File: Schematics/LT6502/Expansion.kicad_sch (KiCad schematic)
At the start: 5 parts, among them J9 DIN41612_02x32_AC

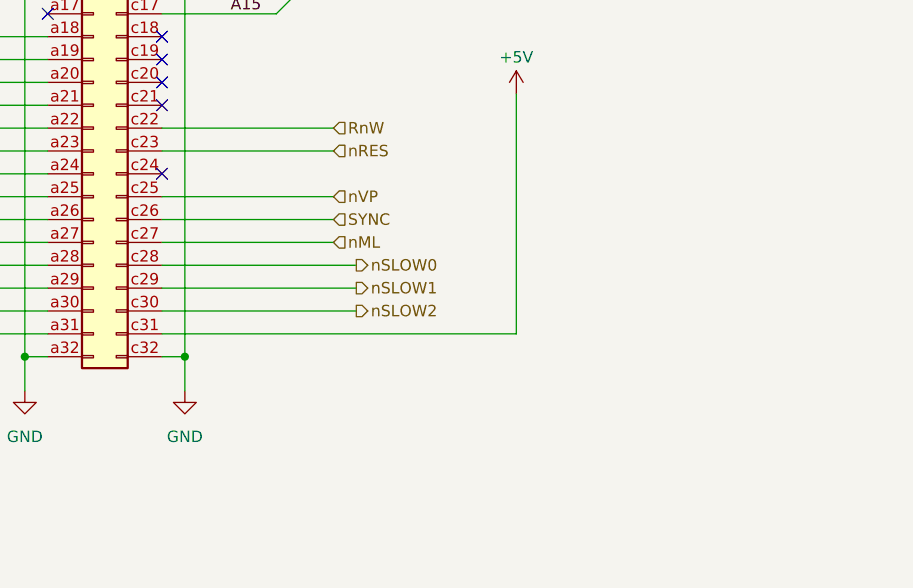
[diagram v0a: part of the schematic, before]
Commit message: Tweaks to Schematics
Shrunk main PCB
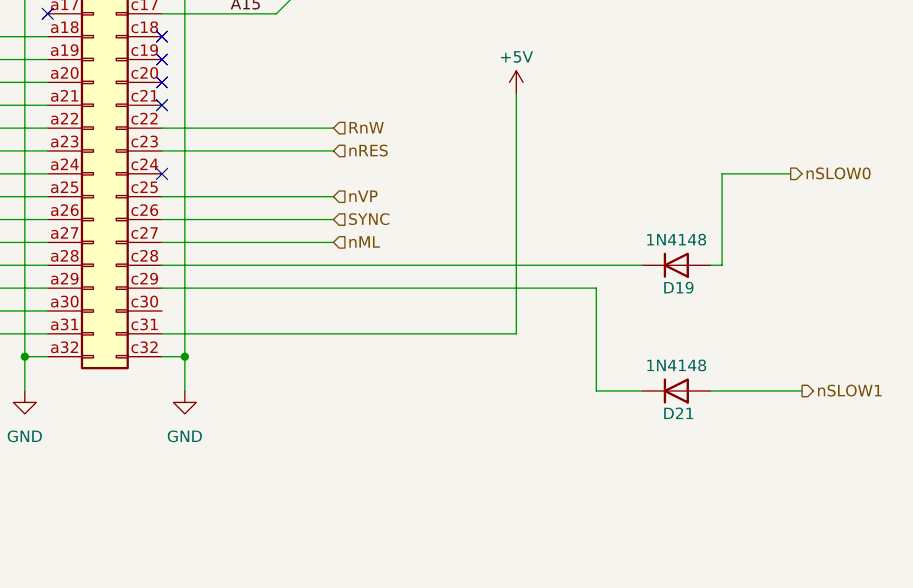
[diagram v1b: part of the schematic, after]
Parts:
- added D19, D21: 1N4148, Diode_THT:D_DO-35_SOD27_P7.62mm_Horizontal, symbol Diode:1N4148
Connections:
- net nSLOW0: now also D19.2 (A); no longer J9.c28 (Pin_c28)
- net nSLOW1: now also D21.2 (A); no longer J9.c29 (Pin_c29)
- net nSLOW2: no longer names the net of J9.c30 (Pin_c30)
- new net: D21.1 (K), J9.c29 (Pin_c29)
- new net: D19.1 (K), J9.c28 (Pin_c28)
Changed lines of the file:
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@@
 	(wire
 		(pts
-			(xy 182.88 124.46) (xy 161.29 124.46)
+			(xy 231.14 114.3) (xy 223.52 114.3)
 		)
 		(stroke
@@
 		)
 	)
-	(wire
-		(pts
-			(xy 182.88 129.54) (xy 161.29 129.54)
-		)
-		(stroke
-			(width 0)
-			(type default)
-		)
-	)
 	(bus
 		(pts
@@
 	(wire
 		(pts
-			(xy 182.88 127) (xy 161.29 127)
+			(xy 232.41 138.43) (xy 222.25 138.43)
 		)
 		(stroke
@@
 	(wire
 		(pts
+			(xy 209.55 138.43) (xy 209.55 127)
+		)
+		(stroke
+			(width 0)
+			(type default)
+		)
+	)
+	(wire
+		(pts
 			(xy 161.29 134.62) (xy 163.83 134.62)
 		)
@@
 	(wire
 		(pts
+			(xy 209.55 127) (xy 161.29 127)
+		)
+		(stroke
+			(width 0)
+			(type default)
+		)
+	)
+	(wire
+		(pts
 			(xy 163.83 134.62) (xy 163.83 55.88)
 		)
@@
 	(wire
 		(pts
+			(xy 214.63 124.46) (xy 161.29 124.46)
+		)
+		(stroke
+			(width 0)
+			(type default)
+		)
+	)
+	(wire
+		(pts
 			(xy 148.59 71.12) (xy 133.35 71.12)
 		)
@@
 	(wire
 		(pts
+			(xy 214.63 138.43) (xy 209.55 138.43)
+		)
+		(stroke
+			(width 0)
+			(type default)
+		)
+	)
+	(wire
+		(pts
 			(xy 180.34 119.38) (xy 161.29 119.38)
 		)
@@
 		)
 	)
+	(wire
+		(pts
+			(xy 223.52 114.3) (xy 223.52 124.46)
+		)
+		(stroke
+			(width 0)
+			(type default)
+		)
+	)
 	(bus
 		(pts
@@
 		(pts
 			(xy 133.35 111.76) (xy 148.59 111.76)
+		)
+		(stroke
+			(width 0)
+			(type default)
+		)
+	)
+	(wire
+		(pts
+			(xy 223.52 124.46) (xy 222.25 124.46)
 		)
 		(stroke
@@
 	(hierarchical_label "nSLOW0"
 		(shape output)
-		(at 182.88 124.46 0)
+		(at 231.14 114.3 0)
 		(effects
 			(font
@@
 	(hierarchical_label "nSLOW1"
 		(shape output)
-		(at 182.88 127 0)
+		(at 232.41 138.43 0)
 		(effects
 			(font
@@
 			)
 			(justify right)
-		)
-	)
-	(hierarchical_label "nSLOW2"
-		(shape output)
-		(at 182.88 129.54 0)
-		(effects
-			(font
-				(size 1.27 1.27)
-			)
-			(justify left)
 		)
 	)
@@
 	)
 	(symbol
+		(lib_id "Diode:1N4148")
+		(at 218.44 138.43 0)
+		(mirror x)
+		(unit 1)
+		(exclude_from_sim no)
+		(in_bom yes)
+		(on_board yes)
+		(dnp no)
+		(property "Reference" "D21"
+			(at 218.694 140.97 0)
+			(effects
+				(font
+					(size 1.27 1.27)
+				)
+			)
+		)
+		(property "Value" "1N4148"
+			(at 218.44 135.636 0)
+			(effects
+				(font
+					(size 1.27 1.27)
+				)
+			)
+		)
+		(property "Footprint" "Diode_THT:D_DO-35_SOD27_P7.62mm_Horizontal"
+			(at 218.44 138.43 0)
+			(effects
+				(font
+					(size 1.27 1.27)
+				)
+				(hide yes)
+			)
+		)
+		(property "Datasheet" "https://assets.nexperia.com/documents/data-sheet/1N4148_1N4448.pdf"
+			(at 218.44 138.43 0)
+			(effects
+				(font
+					(size 1.27 1.27)
+				)
+				(hide yes)
+			)
+		)
+		(property "Description" "100V 0.15A standard switching diode, DO-35"
+			(at 218.44 138.43 0)
+			(effects
+				(font
+					(size 1.27 1.27)
+				)
+				(hide yes)
+			)
+		)
+		(property "Sim.Device" "D"
+			(at 218.44 138.43 0)
+			(effects
+				(font
+					(size 1.27 1.27)
+				)
+				(hide yes)
+			)
+		)
+		(property "Sim.Pins" "1=K 2=A"
+			(at 218.44 138.43 0)
+			(effects
+				(font
+					(size 1.27 1.27)
+				)
+				(hide yes)
+			)
+		)
+		(pin "2"
+		)
+		(pin "1"
+		)
+		(instances
+			(project "LT6502"
+				(path "/a2243a34-697c-4939-97f7-df548e421864/813c43d1-5652-442b-96d1-062e6d70605b"
+					(reference "D22")
+					(unit 1)
+				)
+				(path "/a2243a34-697c-4939-97f7-df548e421864/e762d4e1-6eae-4d69-baef-1dedfb10bbd7"
+					(reference "D21")
+					(unit 1)
+				)
+			)
+		)
+	)
+	(symbol
 		(lib_id "Connector:DIN41612_02x32_AC")
 		(at 153.67 93.98 0)
@@
 					(unit 1)
 				)
+			)
+		)
+	)
+	(symbol
+		(lib_id "Diode:1N4148")
+		(at 218.44 124.46 0)
+		(mirror x)
+		(unit 1)
+		(exclude_from_sim no)
+		(in_bom yes)
+		(on_board yes)
+		(dnp no)
+		(property "Reference" "D19"
+			(at 218.694 127 0)
+			(effects
+				(font
+					(size 1.27 1.27)
+				)
+			)
+		)
+		(property "Value" "1N4148"
+			(at 218.44 121.666 0)
+			(effects
+				(font
+					(size 1.27 1.27)
+				)
+			)
+		)
+		(property "Footprint" "Diode_THT:D_DO-35_SOD27_P7.62mm_Horizontal"
+			(at 218.44 124.46 0)
+			(effects
+				(font
+					(size 1.27 1.27)
+				)
+				(hide yes)
+			)
+		)
+		(property "Datasheet" "https://assets.nexperia.com/documents/data-sheet/1N4148_1N4448.pdf"
+			(at 218.44 124.46 0)
+			(effects
+				(font
+					(size 1.27 1.27)
+				)
+				(hide yes)
+			)
+		)
+		(property "Description" "100V 0.15A standard switching diode, DO-35"
+			(at 218.44 124.46 0)
+			(effects
+				(font
+					(size 1.27 1.27)
+				)
+				(hide yes)
+			)
+		)
+		(property "Sim.Device" "D"
+			(at 218.44 124.46 0)
+			(effects
+				(font
+					(size 1.27 1.27)
+				)
+				(hide yes)
+			)
+		)
+		(property "Sim.Pins" "1=K 2=A"
+			(at 218.44 124.46 0)
+			(effects
+				(font
+					(size 1.27 1.27)
+				)
+				(hide yes)
+			)
+		)
+		(pin "2"
+		)
+		(pin "1"
+		)
+		(instances
+			(project "LT6502"
+				(path "/a2243a34-697c-4939-97f7-df548e421864/813c43d1-5652-442b-96d1-062e6d70605b"
+					(reference "D20")
+					(unit 1)
+				)
+				(path "/a2243a34-697c-4939-97f7-df548e421864/e762d4e1-6eae-4d69-baef-1dedfb10bbd7"
+					(reference "D19")
+					(unit 1)
+				)

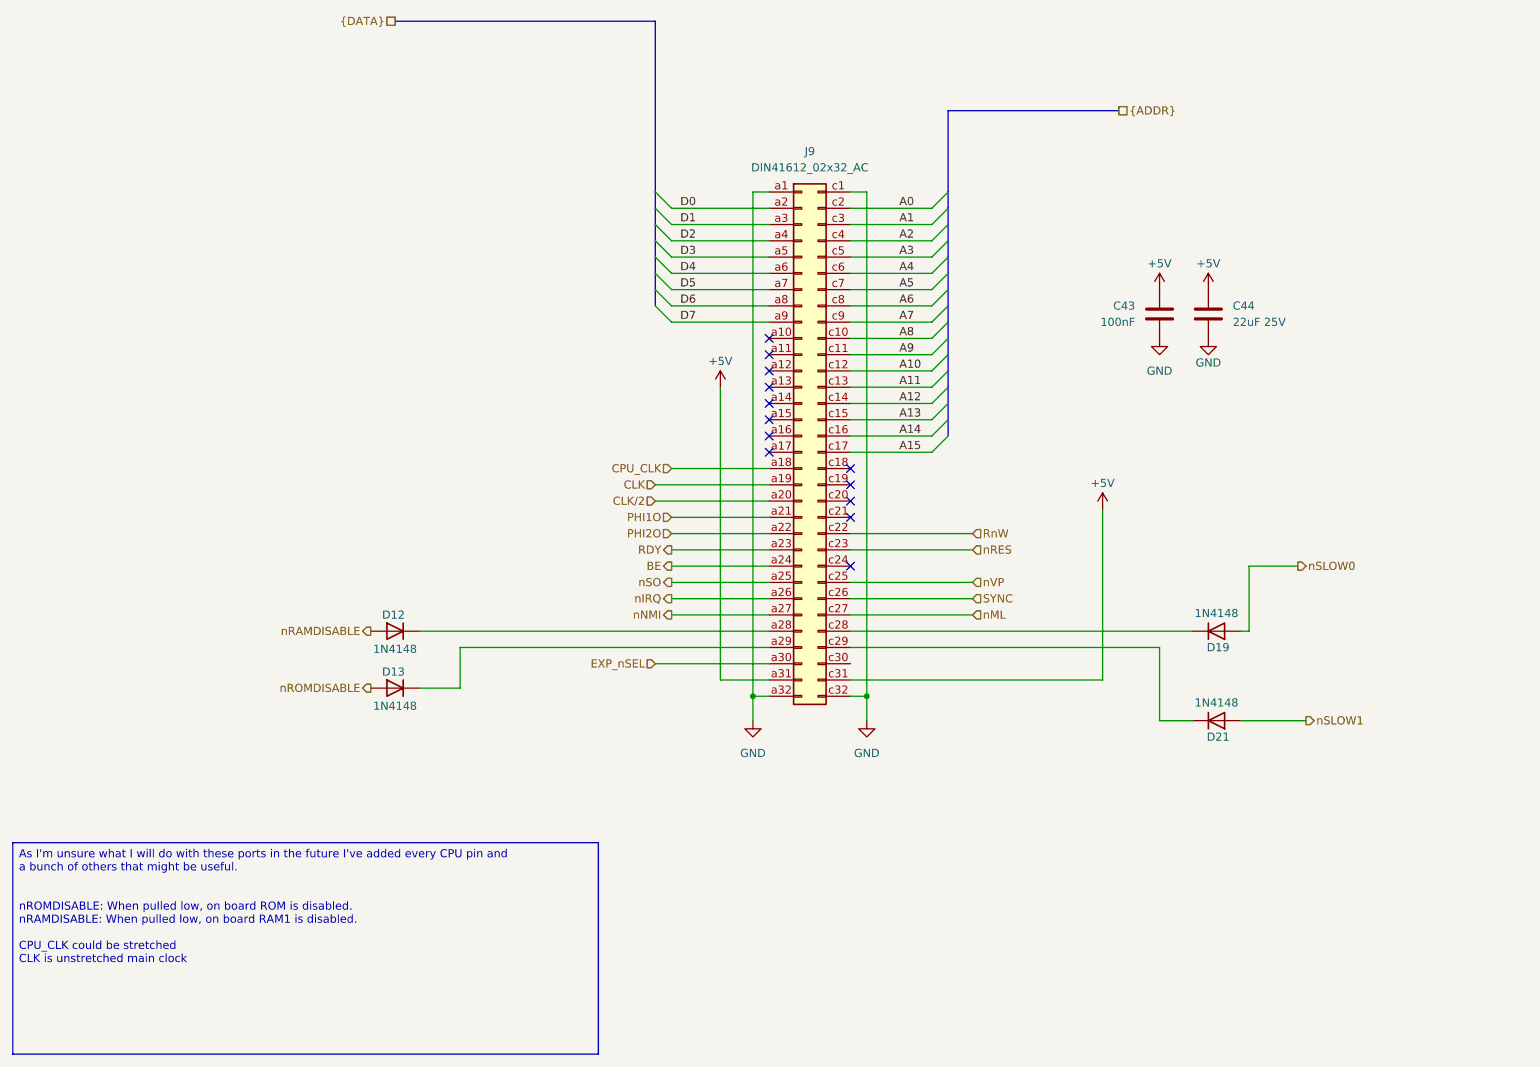
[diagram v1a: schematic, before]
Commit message: Updated main board and started keybed
main board a bit wider due to keybed width
created keybed, begun routing
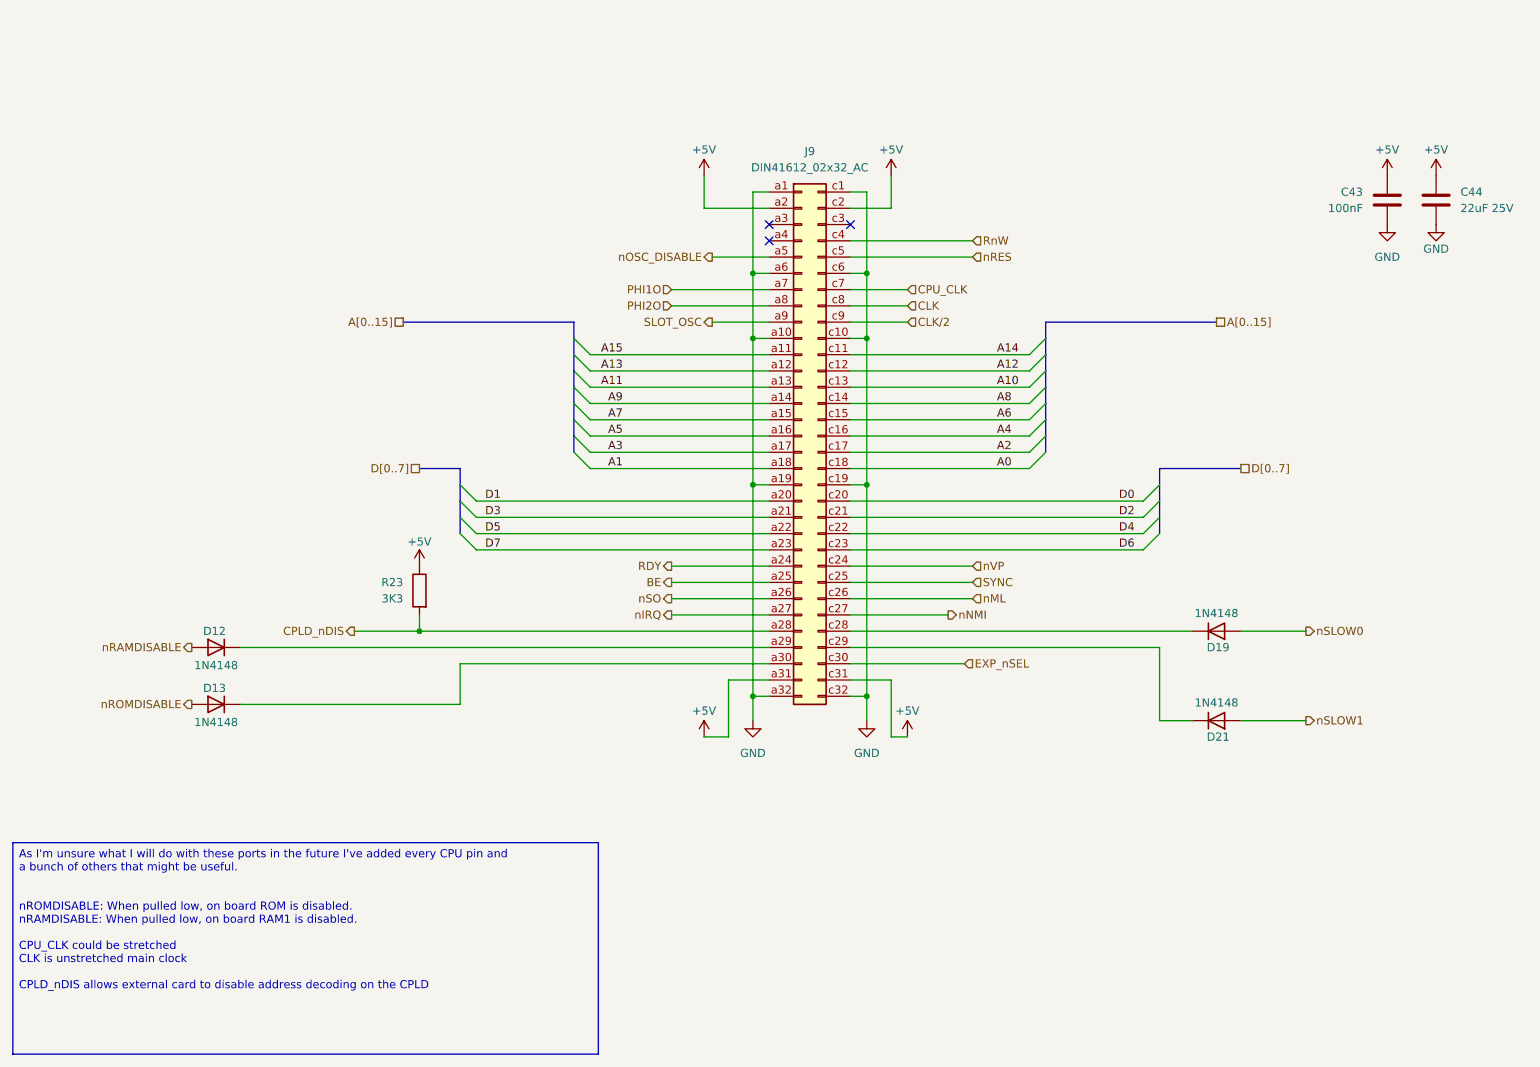
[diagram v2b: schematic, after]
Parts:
- added R23: 3K3, Resistor_SMD:R_0402_1005Metric, symbol Device:R
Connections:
- net +5V: now also J9.a2 (Pin_a2), J9.c2 (Pin_c2), R23.1
- net A0: now also J9.c18 (Pin_c18); no longer J9.c2 (Pin_c2)
- net A1: now also J9.a18 (Pin_a18); no longer J9.c3 (Pin_c3)
- net A10: now also J9.c13 (Pin_c13); no longer J9.c12 (Pin_c12)
- net A11: now also J9.a13 (Pin_a13); no longer J9.c13 (Pin_c13)
- net A12: now also J9.c12 (Pin_c12); no longer J9.c14 (Pin_c14)
- net A13: now also J9.a12 (Pin_a12); no longer J9.c15 (Pin_c15)
- net A14: now also J9.c11 (Pin_c11); no longer J9.c16 (Pin_c16)
- net A15: now also J9.a11 (Pin_a11); no longer J9.c17 (Pin_c17)
- net A2: now also J9.c17 (Pin_c17); no longer J9.c4 (Pin_c4)
- net A3: now also J9.a17 (Pin_a17); no longer J9.c5 (Pin_c5)
- net A4: now also J9.c16 (Pin_c16); no longer J9.c6 (Pin_c6)
- net A5: now also J9.a16 (Pin_a16); no longer J9.c7 (Pin_c7)
- net A6: now also J9.c15 (Pin_c15); no longer J9.c8 (Pin_c8)
- net A7: now also J9.a15 (Pin_a15); no longer J9.c9 (Pin_c9)
- net A8: now also J9.c14 (Pin_c14); no longer J9.c10 (Pin_c10)
- net A9: now also J9.a14 (Pin_a14); no longer J9.c11 (Pin_c11)
- net BE: now also J9.a25 (Pin_a25); no longer J9.a24 (Pin_a24)
- net CLK: now also J9.c8 (Pin_c8); no longer J9.a19 (Pin_a19)
- net CLK/2: now also J9.c9 (Pin_c9); no longer J9.a20 (Pin_a20)
- net CPU_CLK: now also J9.c7 (Pin_c7); no longer J9.a18 (Pin_a18)
- net D0: now also J9.c20 (Pin_c20); no longer J9.a2 (Pin_a2)
- net D1: now also J9.a20 (Pin_a20); no longer J9.a3 (Pin_a3)
- net D2: now also J9.c21 (Pin_c21); no longer J9.a4 (Pin_a4)
- net D3: now also J9.a21 (Pin_a21); no longer J9.a5 (Pin_a5)
- net D4: now also J9.c22 (Pin_c22); no longer J9.a6 (Pin_a6)
- net D5: now also J9.a22 (Pin_a22); no longer J9.a7 (Pin_a7)
- net D6: now also J9.c23 (Pin_c23); no longer J9.a8 (Pin_a8)
- net D7: now also J9.a23 (Pin_a23); no longer J9.a9 (Pin_a9)
- net EXP_nSEL: now also J9.c30 (Pin_c30); no longer J9.a30 (Pin_a30)
- net GND: now also J9.a10 (Pin_a10), J9.a19 (Pin_a19), J9.a6 (Pin_a6), J9.c10 (Pin_c10), J9.c19 (Pin_c19), J9.c6 (Pin_c6)
- net PHI1O: now also J9.a7 (Pin_a7); no longer J9.a21 (Pin_a21)
- net PHI2O: now also J9.a8 (Pin_a8); no longer J9.a22 (Pin_a22)
- net RDY: now also J9.a24 (Pin_a24); no longer J9.a23 (Pin_a23)
- net RnW: now also J9.c4 (Pin_c4); no longer J9.c22 (Pin_c22)
- net SYNC: now also J9.c25 (Pin_c25); no longer J9.c26 (Pin_c26)
- net nIRQ: now also J9.a27 (Pin_a27); no longer J9.a26 (Pin_a26)
- net nML: now also J9.c26 (Pin_c26); no longer J9.c27 (Pin_c27)
- net nNMI: now also J9.c27 (Pin_c27); no longer J9.a27 (Pin_a27)
- net nRES: now also J9.c5 (Pin_c5); no longer J9.c23 (Pin_c23)
- net nSO: now also J9.a26 (Pin_a26); no longer J9.a25 (Pin_a25)
- net nVP: now also J9.c24 (Pin_c24); no longer J9.c25 (Pin_c25)
- net at D12.1 (K): now also J9.a29 (Pin_a29); no longer J9.a28 (Pin_a28)
- net at D13.1 (K): now also J9.a30 (Pin_a30); no longer J9.a29 (Pin_a29)
- new net CPLD_nDIS: J9.a28 (Pin_a28), R23.2
- new net SLOT_OSC: J9.a9 (Pin_a9)
- new net nOSC_DISABLE: J9.a5 (Pin_a5)
- no-connect marks 13 -> 3
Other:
- moved on the sheet: C43, C44, D12, D13
